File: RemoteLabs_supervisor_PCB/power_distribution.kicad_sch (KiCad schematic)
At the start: 31 parts, among them J29 3V3 PWR SRC, J3 XT60_connector_DC_60A_male, J30 12V_DC, J31 5V_DC, J32 GND_BUS, J33 12V_BUS, J34 5V_P_BUS, J35 5V_D_BUS, J36 3V3_BUS, J4 Strip Lighting, J5 USB_A_Stacked, Q1 IRF5305_PBF, U1 LM2596S DC-DC Module, U2 LM2596S DC-DC Module, U3 AMS1117-3.3

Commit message: Stocktaking
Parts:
- removed U2: LM2596S DC-DC Module, Package_TO_SOT_SMD:TO-263-5_TabPin3, symbol 000_Modules_Immo:LM2596S DC-DC Module
- added C1: 10u, Capacitor_SMD:C_0805_2012Metric_Pad1.18x1.45mm_HandSolder, symbol 000_Capacitor_Film_Immo:cap_film_0805
- added C2: 22u, Capacitor_SMD:C_0805_2012Metric_Pad1.18x1.45mm_HandSolder, symbol 000_Capacitor_Film_Immo:cap_film_0805
- added U18: R-78C5.0-1.0, Converter_DCDC:Converter_DCDC_RECOM_R-78E-0.5_THT, symbol Regulator_Switching:R-78C5.0-1.0
- renumbered U1 to A5
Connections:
- net 12V_DC_OUT: now also D6.2 (A), C1.1, U18.1 (IN); no longer D6.1 (K)
- net 3V3_DC_MCU: now also D7.2 (A); no longer D7.1 (K)
- net 5V_DC_SERVO: now also EC10.1, C2.1, U18.3 (OUT); no longer EC10.2
- net GND_P: now also EC10.2, C1.2, C2.2, U18.2 (GND); no longer EC10.1
- net at R36.2: now also D6.1 (K); no longer D6.2 (A)
- net at R37.2: now also D7.1 (K); no longer D7.2 (A)
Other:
- moved on the sheet: D6, D7, EC10

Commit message: Problems with power consumption
Added additional power bus, annoying and expensive but best action
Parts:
- added C?: 10u, Capacitor_SMD:C_0805_2012Metric_Pad1.18x1.45mm_HandSolder, symbol 000_Capacitor_Film_Immo:cap_film_0805
- added C?: 22u, Capacitor_SMD:C_0805_2012Metric_Pad1.18x1.45mm_HandSolder, symbol 000_Capacitor_Film_Immo:cap_film_0805
- added EC?: 100u, Capacitor_SMD:CP_Elec_10x10, symbol 000_Capacitor_Electrolytic_Immo:100u
- added U?: R-78C5.0-1.0, Converter_DCDC:Converter_DCDC_RECOM_R-78E-0.5_THT, symbol Regulator_Switching:R-78C5.0-1.0
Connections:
- net 12V_DC_OUT: now also C?.1, U?.1 (IN)
- net GND_P: now also C?.2, C?.2, EC?.2, U?.2 (GND)
- new net 5V_DC_LED: C?.1, EC?.1, U?.3 (OUT)
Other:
- note added: "All these parts need to be purchased"
- moved on the sheet: A5, C1, C2, D1, D6, D7, EC1, EC10, EC2, EC9, F1, J29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

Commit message: Footprint associations complete
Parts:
- removed TP2: 12V_DC, TestPoint:TestPoint_Pad_D1.5mm, symbol Connector:TestPoint
- removed TP3: 5V_RPI, TestPoint:TestPoint_Pad_D1.5mm, symbol Connector:TestPoint
- removed TP5: 3V3_MCU, TestPoint:TestPoint_Pad_D1.5mm, symbol Connector:TestPoint
- added J6: 5V_DC_LED, TerminalBlock:TerminalBlock_Altech_AK300-2_P5.00mm, symbol Connector:Screw_Terminal_01x02
- D6, D7: footprint (none) -> Diode_SMD:D_0805_2012Metric_Pad1.15x1.40mm_HandSolder
- EC1, EC2: footprint Capacitor_SMD:CP_Elec_6.3x5.9 -> Capacitor_SMD:CP_Elec_4x5.4
- EC10, EC9: footprint Capacitor_SMD:CP_Elec_10x10 -> Capacitor_SMD:CP_Elec_6.3x7.7
- EC12: renamed from EC?; footprint Capacitor_SMD:CP_Elec_10x10 -> Capacitor_SMD:CP_Elec_6.3x7.7
- J31: value 5V_DC -> 5V_DC_RPI
- J5: footprint (none) -> Connector_USB:USB3_A_Molex_48393-001
- gave numbers to parts that had none: 3
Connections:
- net 5V_DC_LED: now also J34.1 (Pin_1), J34.2 (Pin_2), J34.3 (Pin_3), J34.4 (Pin_4), J34.5 (Pin_5), J6.2 (Pin_2)
- net 5V_DC_SERVO: no longer J34.1 (Pin_1), J34.2 (Pin_2), J34.3 (Pin_3), J34.4 (Pin_4), J34.5 (Pin_5)
- net GND_P: now also J6.1 (Pin_1)
- net 5_to_3v3_reg: now reaches EC1.1, J29.2 (Pin_2), JP1.2 (C), U3.3 (VI)
- net 02: now reaches D6.1 (K), R36.2
- net 01: now reaches D1.2 (A), Q1.1 (G), R6.2
- net 12V: now reaches F1.2, Q1.2 (D)
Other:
- moved on the sheet: J34

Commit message: Started PCB layout
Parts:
- A5: footprint Package_TO_SOT_SMD:TO-263-5_TabPin3 -> Module:LM2596S DC-DC Module
- J3: value XT60_connector_DC_60A_male -> XT60_connector_DC_45A_male
- J5: footprint Connector_USB:USB3_A_Molex_48393-001 -> Connector_USB:USB_A_Wuerth_61400826021_Horizontal_Stacked
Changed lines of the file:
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@@
       (effects (font (size 1.27 1.27)) (justify right))
     )
-    (property "Value" "XT60_connector_DC_60A_male" (id 1) (at 43.18 21.59 0)
+    (property "Value" "XT60_connector_DC_45A_male" (id 1) (at 43.18 21.59 0)
       (effects (font (size 1.27 1.27)) (justify right))
     )
@@
     (property "Reference" "A5" (id 0) (at 134.62 57.15 0))
     (property "Value" "LM2596S DC-DC Module" (id 1) (at 134.62 59.69 0))
-    (property "Footprint" "Package_TO_SOT_SMD:TO-263-5_TabPin3" (id 2) (at 147.32 85.09 0)
+    (property "Footprint" "Module:LM2596S DC-DC Module" (id 2) (at 147.32 85.09 0)
       (effects (font (size 1.27 1.27) italic) (justify left) hide)
     )
@@
       (effects (font (size 1.27 1.27)) (justify right))
     )
-    (property "Footprint" "Connector_USB:USB3_A_Molex_48393-001" (id 2) (at 239.395 66.04 0)
+    (property "Footprint" "Connector_USB:USB_A_Wuerth_61400826021_Horizontal_Stacked" (id 2) (at 239.395 66.04 0)
       (effects (font (size 1.27 1.27)) (justify left) hide)
     )

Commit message: PCB layout
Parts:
- removed TP4: 5V_SERVO, TestPoint:TestPoint_Pad_D1.5mm, symbol Connector:TestPoint
- J3: value XT60_connector_DC_45A_male -> XT60_60A_male; symbol 000_Connectors_Immo:XT60_connector_DC_60A_male -> 000_Connectors_Immo:XT60_60A_male
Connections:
- no-connect marks 4 -> 6
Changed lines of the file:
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@@
   (no_connect (at 233.045 54.61))
   (no_connect (at 233.045 57.15))
+  (no_connect (at 26.035 33.02))
+  (no_connect (at 26.035 35.56))
   (wire (pts (xy 221.615 86.995) (xy 221.615 88.265))
     (stroke (width 0) (type default) (color 0 0 0 0))
   )
-  (wire (pts (xy 168.91 150.495) (xy 168.91 153.035))
-    (stroke (width 0) (type default) (color 0 0 0 0))
-  )
   (wire (pts (xy 143.51 113.665) (xy 150.495 113.665))
     (stroke (width 0) (type default) (color 0 0 0 0))
@@
     (stroke (width 0) (type default) (color 0 0 0 0))
   )
+  (wire (pts (xy 24.13 35.56) (xy 26.035 35.56))
+    (stroke (width 0) (type default) (color 0 0 0 0))
+  )
   (wire (pts (xy 163.83 125.73) (xy 177.165 125.73))
     (stroke (width 0) (type default) (color 0 0 0 0))
@@
   )
   (wire (pts (xy 191.135 95.885) (xy 191.135 97.155))
+    (stroke (width 0) (type default) (color 0 0 0 0))
+  )
+  (wire (pts (xy 24.13 33.02) (xy 26.035 33.02))
     (stroke (width 0) (type default) (color 0 0 0 0))
   )
@@
     (pin "3")
   )
-  (symbol (lib_id "000_Connectors_Immo:XT60_connector_DC_60A_male") (at 21.59 29.21 0) (mirror x) (unit 1)
+  (symbol (lib_id "000_Connectors_Immo:XT60_60A_male") (at 21.59 27.305 0) (unit 1)
     (in_bom yes) (on_board yes)
-    (property "Reference" "J3" (id 0) (at 17.78 19.05 0)
+    (property "Reference" "J3" (id 0) (at 19.685 19.05 0)
       (effects (font (size 1.27 1.27)) (justify right))
     )
-    (property "Value" "XT60_connector_DC_45A_male" (id 1) (at 43.18 21.59 0)
+    (property "Value" "XT60_60A_male" (id 1) (at 31.115 22.225 0)
       (effects (font (size 1.27 1.27)) (justify right))
     )
@@
     (pin "1")
     (pin "2")
+    (pin "S1")
+    (pin "S2")
   )
   (symbol (lib_id "Connector:Screw_Terminal_01x02") (at 182.245 123.19 0) (unit 1)
@@
     (pin "5")
   )
-  (symbol (lib_id "Connector:TestPoint") (at 168.91 150.495 0) (unit 1)
-    (in_bom yes) (on_board yes)
-    (property "Reference" "TP4" (id 0) (at 172.72 149.225 0)
-      (effects (font (size 1.27 1.27)) (justify right))
-    )
-    (property "Value" "5V_SERVO" (id 1) (at 175.26 145.415 0)
-      (effects (font (size 1.27 1.27)) (justify right))
-    )
-    (property "Footprint" "TestPoint:TestPoint_Pad_D1.5mm" (id 2) (at 173.99 150.495 0)
-      (effects (font (size 1.27 1.27)) hide)
-    )
-    (property "Datasheet" "~" (id 3) (at 173.99 150.495 0)
-      (effects (font (size 1.27 1.27)) hide)
-    )
-    (pin "1")
-  )
   (symbol (lib_id "000_Capacitor_Film_Immo:cap_film_0805") (at 143.51 120.015 0) (unit 1)

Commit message: PCB layout
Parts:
- J4: footprint Connector_PinHeader_1.27mm:PinHeader_1x02_P1.27mm_Vertical -> Connector_Molex:Molex_KK-254_AE-6410-02A_1x02_P2.54mm_Vertical; symbol 000_Pin_Headers_Immo:Conn_01x02_Male -> 000_Connectors_Immo:2pin_molex_2.54mm_male
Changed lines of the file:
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@@
     (pin "2")
   )
-  (symbol (lib_id "000_Pin_Headers_Immo:Conn_01x02_Male") (at 187.96 33.02 180) (unit 1)
+  (symbol (lib_id "000_Connectors_Immo:2pin_molex_2.54mm_male") (at 187.96 33.02 180) (unit 1)
     (in_bom yes) (on_board yes)
     (property "Reference" "J4" (id 0) (at 189.23 30.4799 0)
@@
       (effects (font (size 1.27 1.27)) (justify right))
     )
-    (property "Footprint" "Connector_PinHeader_1.27mm:PinHeader_1x02_P1.27mm_Vertical" (id 2) (at 187.96 33.02 0)
+    (property "Footprint" "Connector_Molex:Molex_KK-254_AE-6410-02A_1x02_P2.54mm_Vertical" (id 2) (at 187.96 33.02 0)
       (effects (font (size 1.27 1.27)) hide)
     )

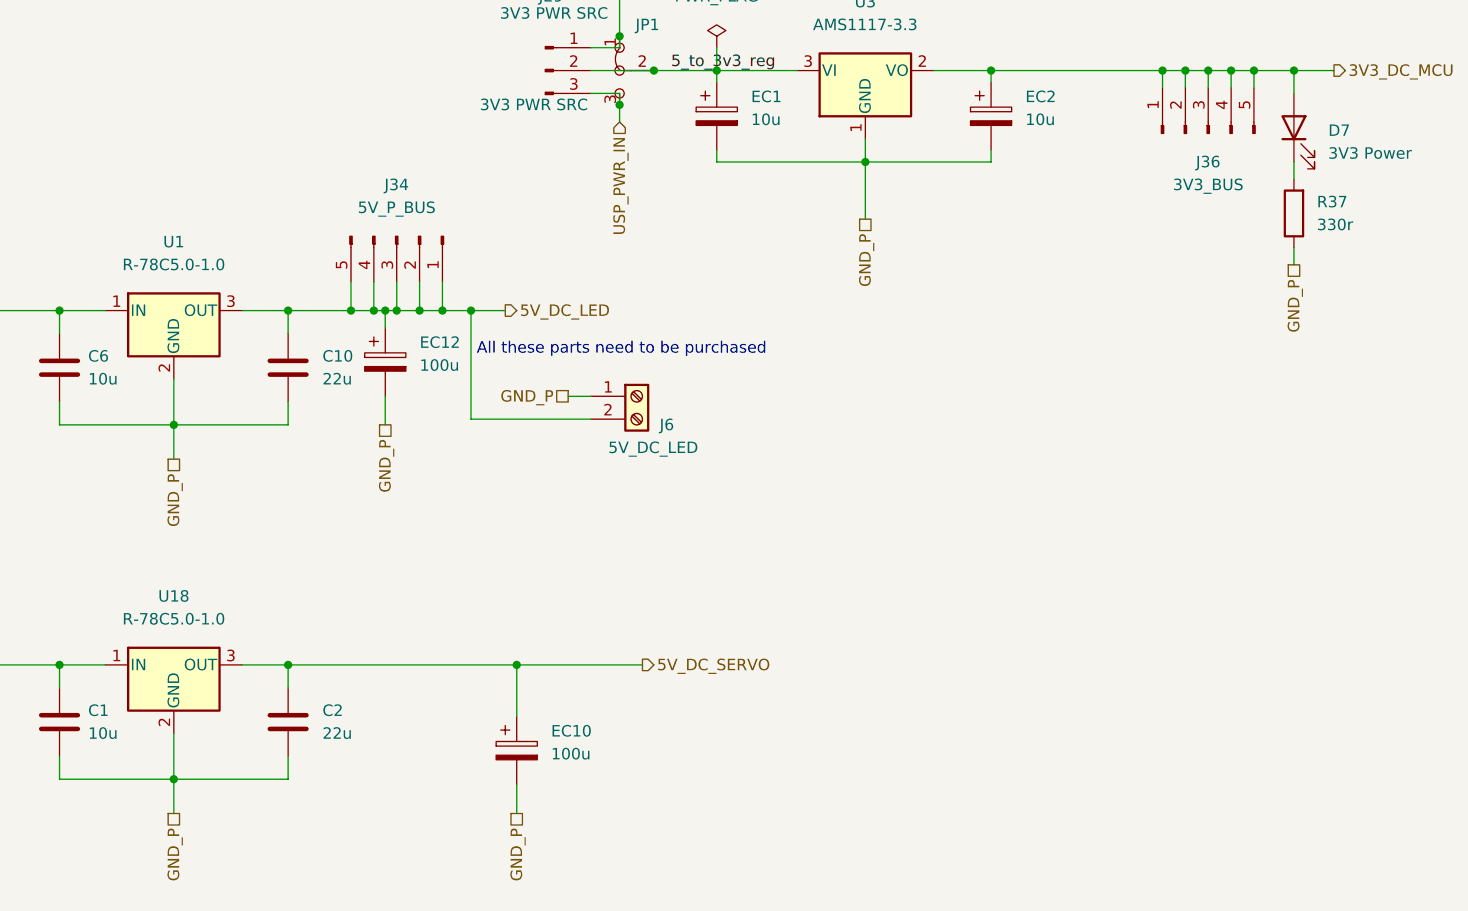
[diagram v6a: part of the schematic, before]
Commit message: version one finished excluding net ties
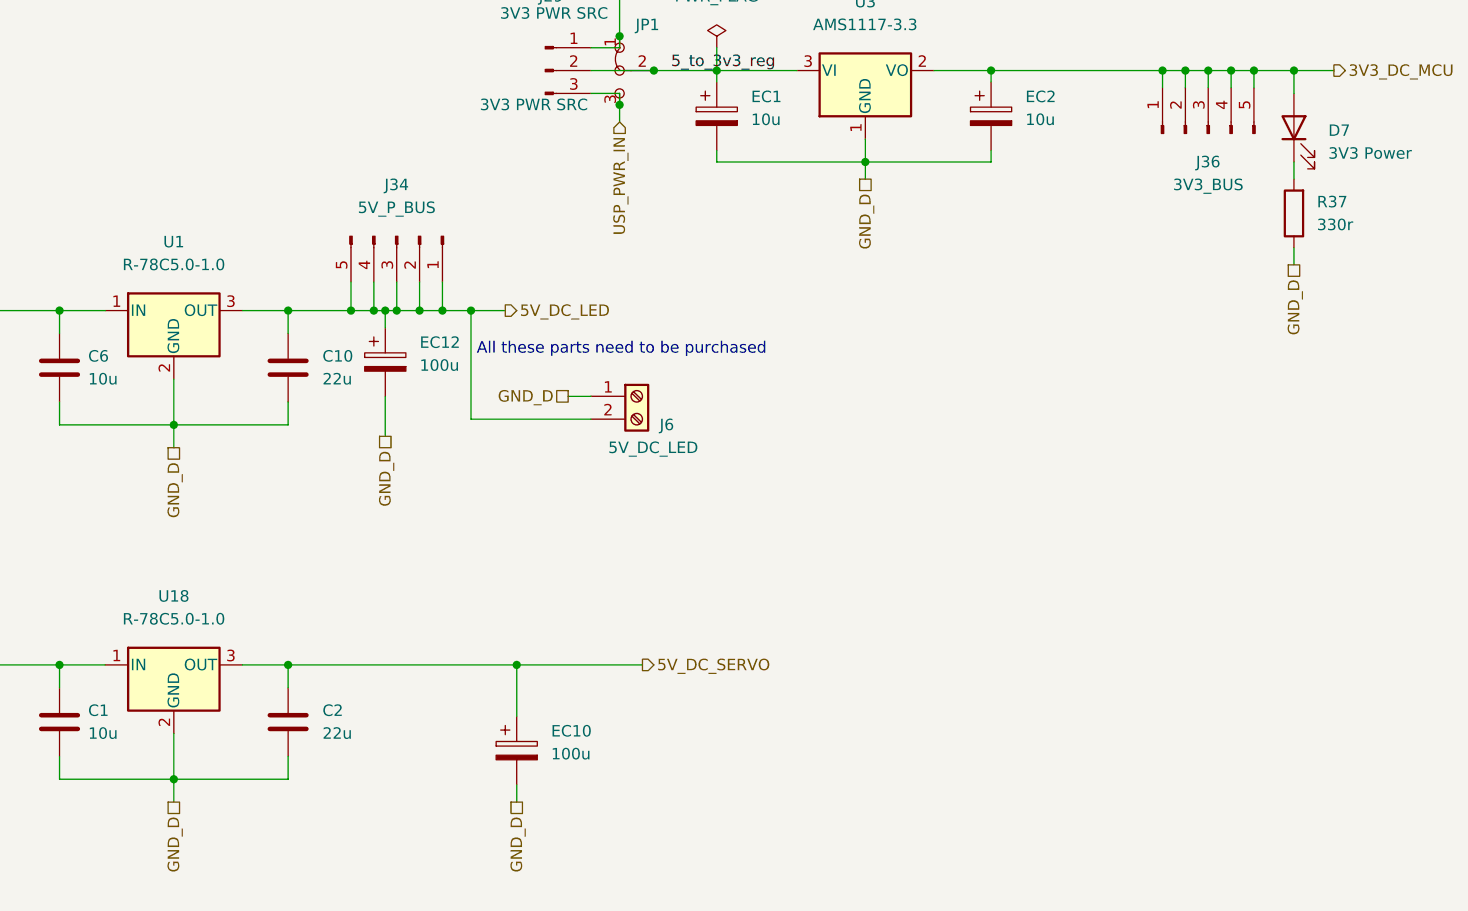
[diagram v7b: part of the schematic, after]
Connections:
- net GND_P: no longer C1.2, C10.2, C2.2, C6.2, EC1.2, EC10.2, EC12.2, EC2.2, J6.1 (Pin_1), R37.1, U1.2 (GND), U18.2 (GND), U3.1 (GND)
- new net GND_D: C1.2, C10.2, C2.2, C6.2, EC1.2, EC10.2, EC12.2, EC2.2, J6.1 (Pin_1), R37.1, U1.2 (GND), U18.2 (GND), U3.1 (GND)
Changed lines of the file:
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@@
-    (stroke (width 0) (type default) (color 0 0 0 0))
-  )
-  (wire (pts (xy 154.305 123.19) (xy 154.305 126.365))
     (stroke (width 0) (type default) (color 0 0 0 0))
   )
@@
     (stroke (width 0) (type default) (color 0 0 0 0))
   )
+  (wire (pts (xy 130.81 168.275) (xy 130.81 165.735))
+    (stroke (width 0) (type default) (color 0 0 0 0))
+  )
   (wire (pts (xy 155.575 110.49) (xy 155.575 113.665))
     (stroke (width 0) (type default) (color 0 0 0 0))
@@
     (stroke (width 0) (type default) (color 0 0 0 0))
   )
-  (wire (pts (xy 143.51 165.735) (xy 130.81 165.735))
+  (wire (pts (xy 130.81 165.735) (xy 143.51 165.735))
     (stroke (width 0) (type default) (color 0 0 0 0))
   )
@@
     (stroke (width 0) (type default) (color 0 0 0 0))
   )
-  (wire (pts (xy 168.91 166.37) (xy 168.91 169.545))
-    (stroke (width 0) (type default) (color 0 0 0 0))
-  )
-  (wire (pts (xy 130.81 169.545) (xy 130.81 165.735))
+  (wire (pts (xy 130.81 126.365) (xy 130.81 128.905))
     (stroke (width 0) (type default) (color 0 0 0 0))
   )
@@
     (stroke (width 0) (type default) (color 0 0 0 0))
   )
-  (wire (pts (xy 207.645 97.155) (xy 207.645 103.505))
-    (stroke (width 0) (type default) (color 0 0 0 0))
-  )
   (wire (pts (xy 60.325 103.505) (xy 57.785 103.505))
     (stroke (width 0) (type default) (color 0 0 0 0))
@@
     (stroke (width 0) (type default) (color 0 0 0 0))
   )
+  (wire (pts (xy 174.625 123.19) (xy 177.165 123.19))
+    (stroke (width 0) (type default) (color 0 0 0 0))
+  )
   (wire (pts (xy 218.44 31.75) (xy 218.44 41.91))
     (stroke (width 0) (type default) (color 0 0 0 0))
@@
     (stroke (width 0) (type default) (color 0 0 0 0))
   )
+  (wire (pts (xy 154.305 123.19) (xy 154.305 127.635))
+    (stroke (width 0) (type default) (color 0 0 0 0))
+  )
   (wire (pts (xy 160.655 113.665) (xy 163.83 113.665))
     (stroke (width 0) (type default) (color 0 0 0 0))
@@
     (stroke (width 0) (type default) (color 0 0 0 0))
   )
-  (wire (pts (xy 174.625 123.19) (xy 177.165 123.19))
-    (stroke (width 0) (type default) (color 0 0 0 0))
-  )
   (wire (pts (xy 240.665 88.9) (xy 240.665 86.995))
     (stroke (width 0) (type default) (color 0 0 0 0))
@@
     (stroke (width 0) (type default) (color 0 0 0 0))
   )
+  (wire (pts (xy 255.27 106.68) (xy 255.27 108.585))
+    (stroke (width 0) (type default) (color 0 0 0 0))
+  )
   (wire (pts (xy 65.405 103.505) (xy 67.945 103.505))
     (stroke (width 0) (type default) (color 0 0 0 0))
@@
     (stroke (width 0) (type default) (color 0 0 0 0))
   )
+  (wire (pts (xy 168.91 166.37) (xy 168.91 168.275))
+    (stroke (width 0) (type default) (color 0 0 0 0))
+  )
   (wire (pts (xy 177.8 39.37) (xy 177.8 33.02))
     (stroke (width 0) (type default) (color 0 0 0 0))
@@
     (stroke (width 0) (type default) (color 0 0 0 0))
   )
+  (wire (pts (xy 207.645 97.155) (xy 207.645 99.06))
+    (stroke (width 0) (type default) (color 0 0 0 0))
+  )
   (wire (pts (xy 153.67 24.13) (xy 153.67 26.67))
     (stroke (width 0) (type default) (color 0 0 0 0))
@@
     (stroke (width 0) (type default) (color 0 0 0 0))
   )
-  (wire (pts (xy 130.81 130.175) (xy 130.81 126.365))
-    (stroke (width 0) (type default) (color 0 0 0 0))
-  )
   (wire (pts (xy 65.405 103.505) (xy 65.405 111.125))
     (stroke (width 0) (type default) (color 0 0 0 0))
@@
   )
   (wire (pts (xy 180.34 84.455) (xy 180.34 83.185))
-    (stroke (width 0) (type default) (color 0 0 0 0))
-  )
-  (wire (pts (xy 255.27 106.68) (xy 255.27 108.585))
     (stroke (width 0) (type default) (color 0 0 0 0))
   )
@@
     (effects (font (size 1.27 1.27)) (justify left bottom))
   )
+  (hierarchical_label "GND_D" (shape passive) (at 130.81 128.905 270)
+    (effects (font (size 1.27 1.27)) (justify right))
+  )
+  (hierarchical_label "GND_D" (shape passive) (at 255.27 108.585 270)
+    (effects (font (size 1.27 1.27)) (justify right))
+  )
+  (hierarchical_label "GND_D" (shape passive) (at 168.91 168.275 270)
+    (effects (font (size 1.27 1.27)) (justify right))
+  )
   (hierarchical_label "GND_P" (shape passive) (at 30.48 59.69 270)
     (effects (font (size 1.27 1.27)) (justify right))
@@
     (effects (font (size 1.27 1.27)) (justify left))
   )
+  (hierarchical_label "GND_D" (shape passive) (at 174.625 123.19 180)
+    (effects (font (size 1.27 1.27)) (justify right))
+  )
   (hierarchical_label "5V_DC_RPI" (shape output) (at 184.15 63.5 0)
     (effects (font (size 1.27 1.27)) (justify left))
@@
     (effects (font (size 1.27 1.27)) (justify left))
   )
+  (hierarchical_label "GND_D" (shape passive) (at 207.645 99.06 270)
+    (effects (font (size 1.27 1.27)) (justify right))
+  )
   (hierarchical_label "GND_P" (shape passive) (at 65.405 111.125 270)
     (effects (font (size 1.27 1.27)) (justify right))
   )
-  (hierarchical_label "GND_P" (shape passive) (at 174.625 123.19 180)
-    (effects (font (size 1.27 1.27)) (justify right))
-  )
-  (hierarchical_label "GND_P" (shape passive) (at 207.645 103.505 270)
-    (effects (font (size 1.27 1.27)) (justify right))
-  )
-  (hierarchical_label "GND_P" (shape passive) (at 130.81 130.175 270)
+  (hierarchical_label "GND_D" (shape passive) (at 154.305 127.635 270)
     (effects (font (size 1.27 1.27)) (justify right))
   )
@@
     (effects (font (size 1.27 1.27)) (justify right))
   )
+  (hierarchical_label "GND_D" (shape passive) (at 130.81 168.275 270)
+    (effects (font (size 1.27 1.27)) (justify right))
+  )
   (hierarchical_label "GND_P" (shape passive) (at 152.4 68.58 0)
     (effects (font (size 1.27 1.27)) (justify left))
@@
     (effects (font (size 1.27 1.27)) (justify left))
   )
-  (hierarchical_label "GND_P" (shape passive) (at 255.27 108.585 270)
-    (effects (font (size 1.27 1.27)) (justify right))
-  )
-  (hierarchical_label "GND_P" (shape passive) (at 168.91 169.545 270)
-    (effects (font (size 1.27 1.27)) (justify right))
-  )
-  (hierarchical_label "GND_P" (shape passive) (at 130.81 169.545 270)
-    (effects (font (size 1.27 1.27)) (justify right))
-  )
   (hierarchical_label "GND_P" (shape passive) (at 176.53 33.02 180)
     (effects (font (size 1.27 1.27)) (justify right))
@@
     (effects (font (size 1.27 1.27)) (justify left))
   )
-  (hierarchical_label "GND_P" (shape passive) (at 154.305 126.365 270)
-    (effects (font (size 1.27 1.27)) (justify right))
-  )
   (symbol (lib_id "000_Pin_Headers_Immo:Conn_01x05_Male") (at 151.13 19.05 270) (unit 1)
